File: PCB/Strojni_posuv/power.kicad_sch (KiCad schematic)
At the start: 0 parts

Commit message: PCB making #1 Power management
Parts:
- added 5V1: 5V, TestPoint:TestPoint_Pad_D1.5mm, symbol Connector:TestPoint
- added C15, C16: 1u, Capacitor_SMD:C_0402_1005Metric, symbol Device:C
- added D1: LED, LED_SMD:LED_0603_1608Metric, symbol Device:LED
- added JP1: SolderJumper_2_Open, Jumper:SolderJumper-2_P1.3mm_Open_TrianglePad1.0x1.5mm, symbol Jumper:SolderJumper_2_Open
- added R12: 510, Resistor_SMD:R_0402_1005Metric, symbol Device:R
- added U2: ~, Package_SO:SOIC-8-1EP_3.9x4.9mm_P1.27mm_EP2.29x3mm, symbol MP9486:MP9486AGN-Z
- added U4: MIC5365-3.3YC5, Package_TO_SOT_SMD:SOT-353_SC-70-5, symbol Regulator_Linear:MIC5365-3.3YC5
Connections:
- new net: D1.1 (K), R12.1
- new net: D1.2 (A), JP1.2 (B)
- new net +3.3V: C16.2, JP1.1 (A), U4.5 (VOUT)
- new net +5V: 5V1.1, C15.2, U4.1 (VIN), U4.3 (EN)
- new net GND: C15.1, C16.1, R12.2, U4.2 (GND)
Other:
- note added: "300mA"
- note added: "5V to 3.3V"
- note added: "Power LED"

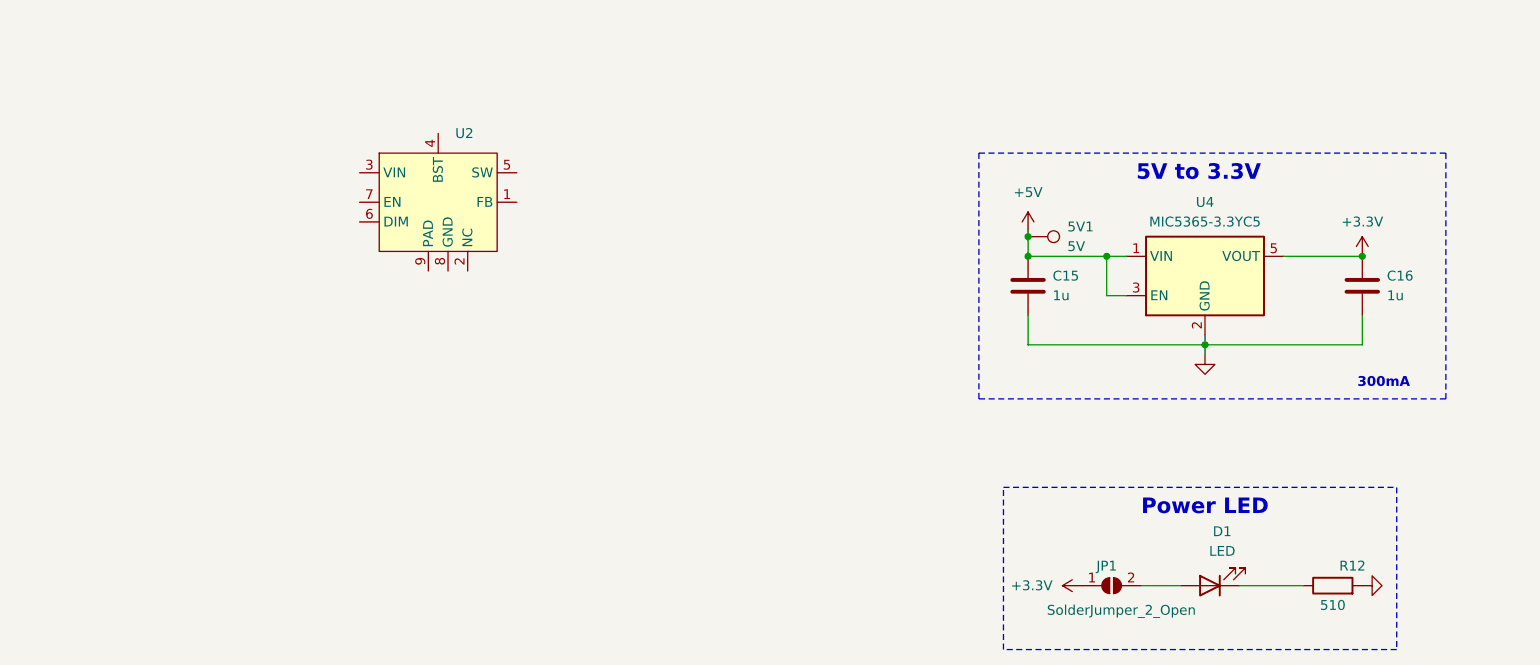
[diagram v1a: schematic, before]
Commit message: Learning, PCB making #2 Added new links to Learning Motor driver part in Kicad, Power part (48V to 5V), New pins to STM32F103
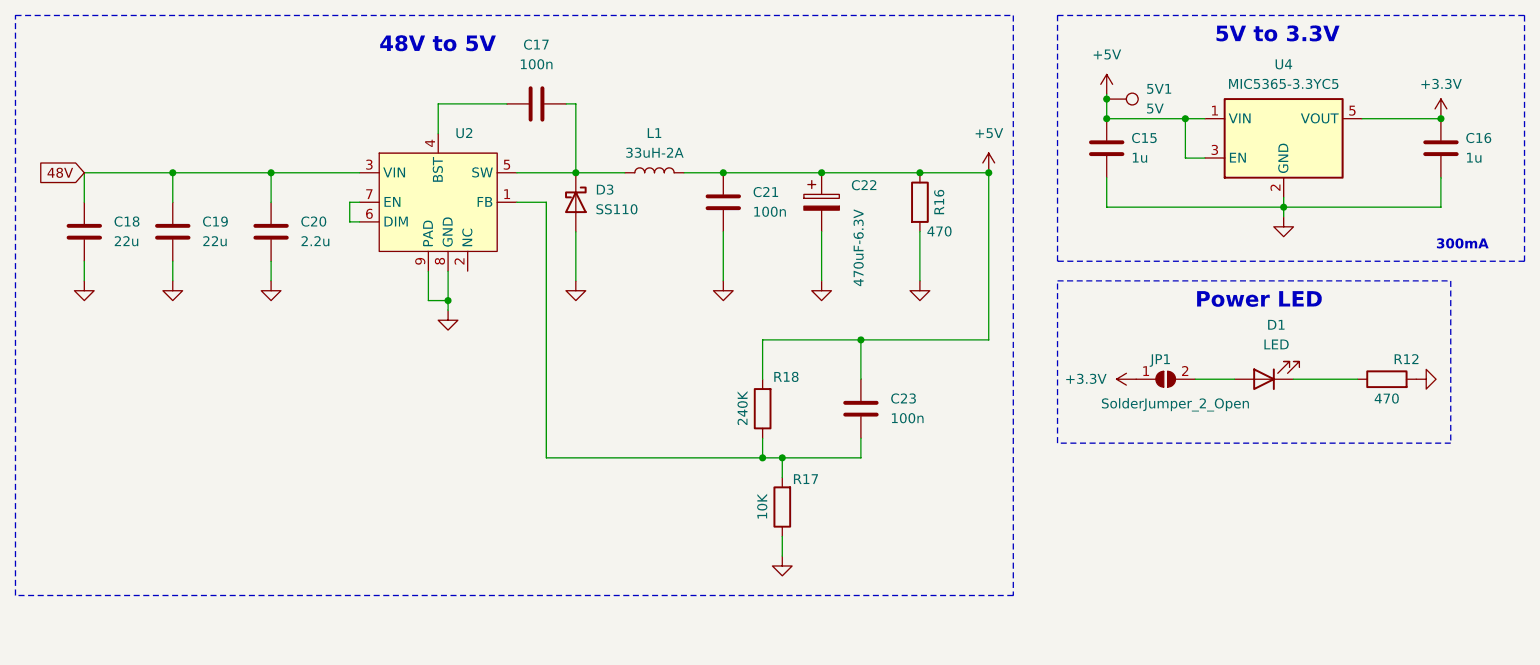
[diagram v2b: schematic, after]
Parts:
- added C17, C21, C23: 100n, symbol Device:C
- added C18, C19: 22u, symbol Device:C
- added C20: 2.2u, symbol Device:C
- added C22: 470uF-6.3V, symbol Device:C_Polarized
- added D3: SS110, symbol Device:D_Schottky
- added L1: 33uH-2A, symbol Device:L
- added R16: 470, symbol Device:R
- added R17: 10K, symbol Device:R
- added R18: 240K, symbol Device:R
- R12: value 510 -> 470
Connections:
- net +5V: now also C21.2, C22.1, C23.2, L1.2, R16.1, R18.2
- net GND: now also U2.8 (GND), U2.9 (PAD), C18.2, C19.2, C20.2, C21.1, C22.2, D3.2 (A), R16.2, R17.1
- net at U2.1 (FB): now also C23.1, R17.2, R18.1
- net 48V: now reaches U2.3 (VIN)
- net 48V: now also C18.1, C19.1, C20.1
- net at U2.4 (BST): now also C17.1
- net at U2.5 (SW): now also C17.2, D3.1 (K), L1.1
- net at U2.6 (DIM): now also U2.7 (EN)
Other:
- note added: "48V to 5V"
- moved on the sheet: 5V1, C15, C16, D1, JP1, R12, U4

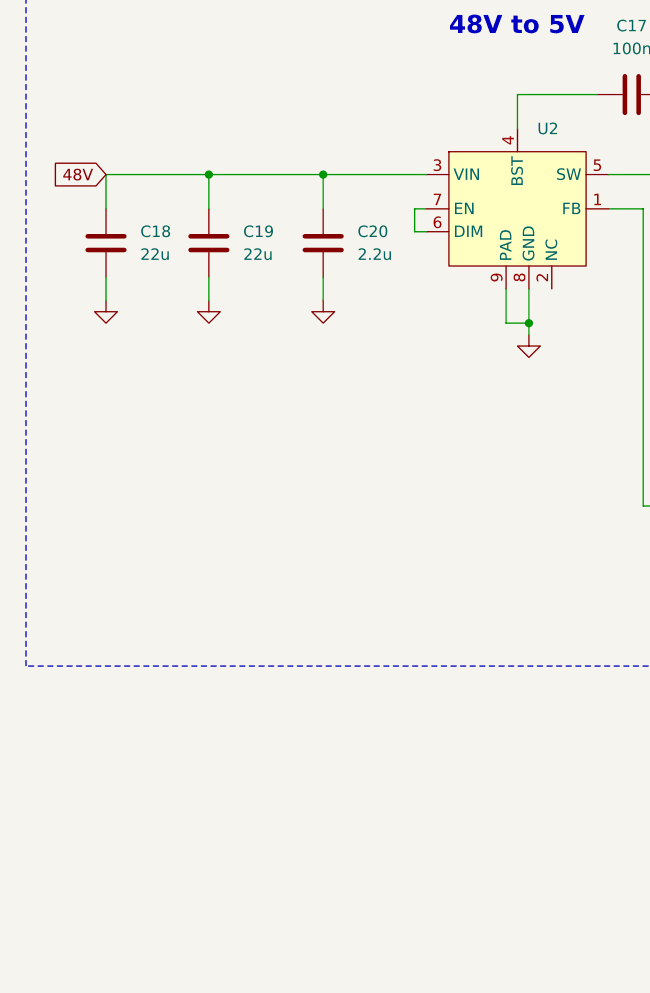
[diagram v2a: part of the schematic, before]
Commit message: PCB making #3 Whole motor driver, small power changes, STM32 clock and new pin configuration
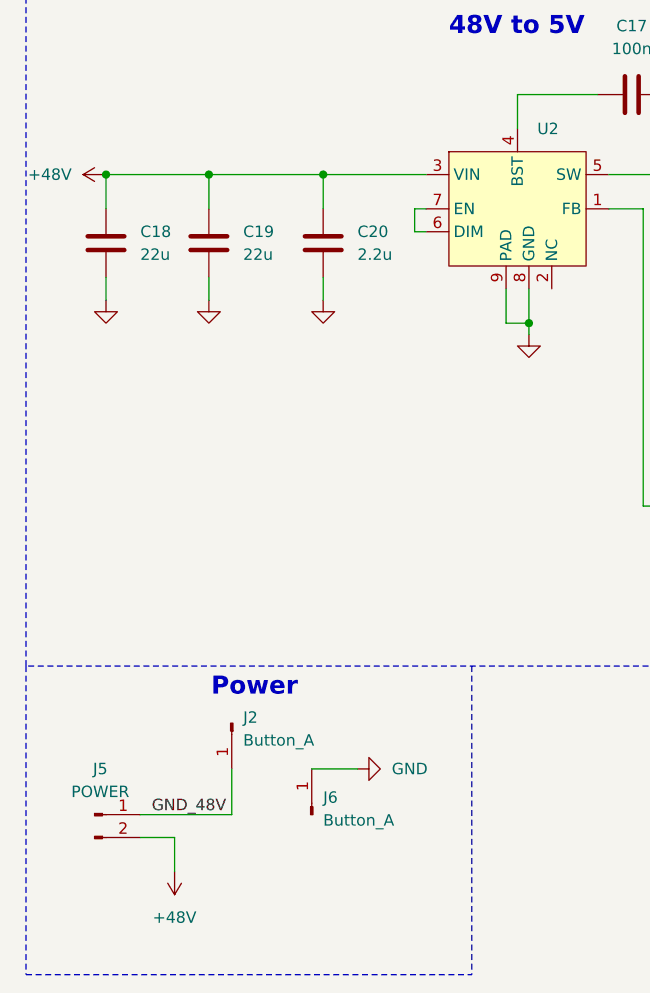
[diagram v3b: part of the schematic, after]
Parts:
- added J2, J6: Button_A, Connector_Pin:Pin_D1.3mm_L11.3mm_W2.8mm_Flat, symbol Connector:Conn_01x01_Pin
- added J5: POWER, Connector_AMASS:AMASS_XT60-M_1x02_P7.20mm_Vertical, symbol Connector:Conn_01x02_Pin
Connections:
- net GND: now also J6.1 (Pin_1)
- net 48V renamed +48V
- net +48V: now also J5.2 (Pin_2)
- new net GND_48V: J2.1 (Pin_1), J5.1 (Pin_1)
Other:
- note added: "Power"

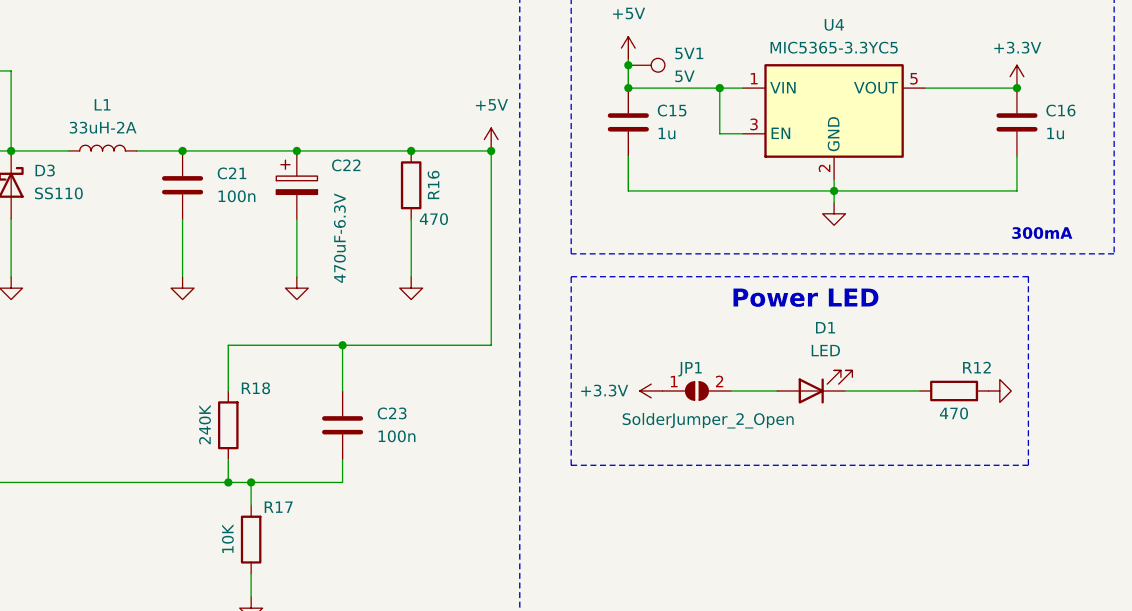
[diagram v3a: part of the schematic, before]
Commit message: PCB making #4 Finding components on JLCPCB and adding their tags to schematic. Assigning almost all footprints
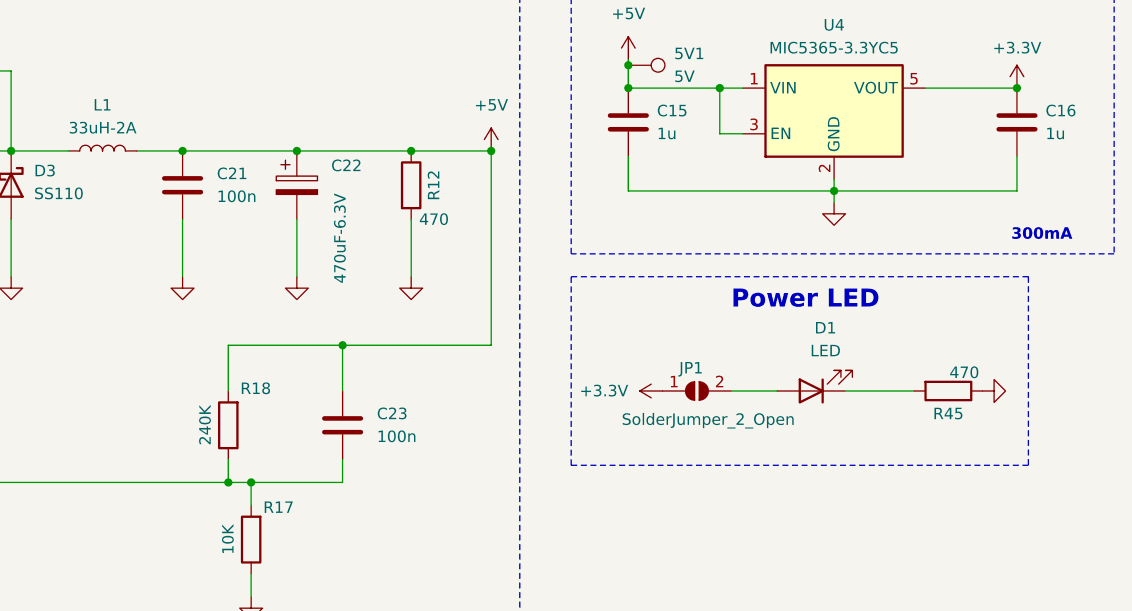
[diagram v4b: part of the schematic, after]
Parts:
- removed R16: 470, symbol Device:R
- added R45: 470, Resistor_SMD:R_0603_1608Metric, symbol Device:R
- C15, C16: footprint Capacitor_SMD:C_0402_1005Metric -> Capacitor_SMD:C_0603_1608Metric; LCSC C412453 -> C15849
- C17, C21, C23: footprint (none) -> Capacitor_SMD:C_0603_1608Metric; LCSC (none) -> C14663
- C18, C19: footprint (none) -> Capacitor_SMD:C_2220_5750Metric; LCSC (none) -> C784103
- C20: footprint (none) -> Capacitor_SMD:C_0805_2012Metric; LCSC (none) -> C513763
- C22: footprint (none) -> Capacitor_SMD:CP_Elec_6.3x7.7; LCSC (none) -> C114446
- D3: footprint (none) -> Diode_SMD:D_SMA; LCSC (none) -> C2482
- L1: footprint (none) -> Inductor_SMD:L_Sunlord_MWSA0603S; LCSC (none) -> C408454
- R12: footprint Resistor_SMD:R_0402_1005Metric -> Resistor_SMD:R_0603_1608Metric; LCSC C103085 -> C23179
- R17: footprint (none) -> Resistor_SMD:R_0603_1608Metric; LCSC (none) -> C25804
- R18: footprint (none) -> Resistor_SMD:R_0603_1608Metric; LCSC (none) -> C4197
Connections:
- net +5V: now also C21.1, C23.1, R12.1; no longer C21.2, C23.2
- net GND: now also C21.2, R45.1; no longer C21.1
- net at R17.2, R18.1, U2.1 (FB): now also C23.2; no longer C23.1
- net at D1.1 (K): now also R45.2; no longer R12.1

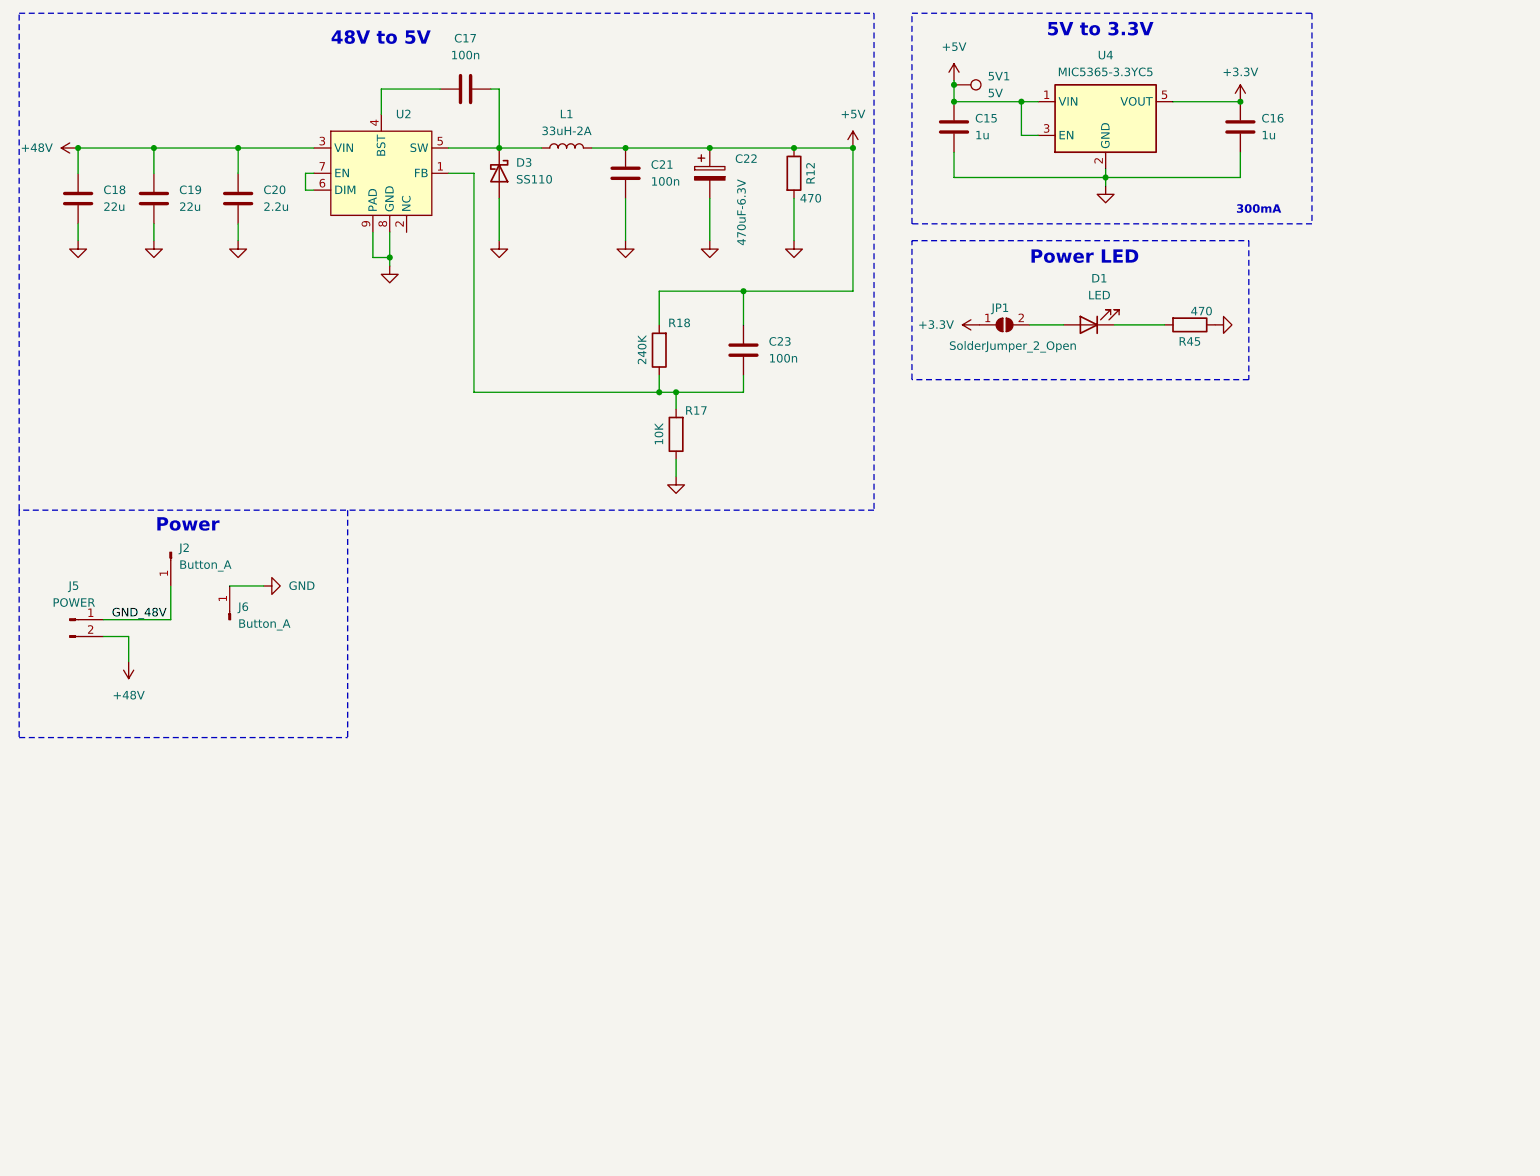
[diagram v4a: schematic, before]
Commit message: PCB making #6 Placing all components - component layout
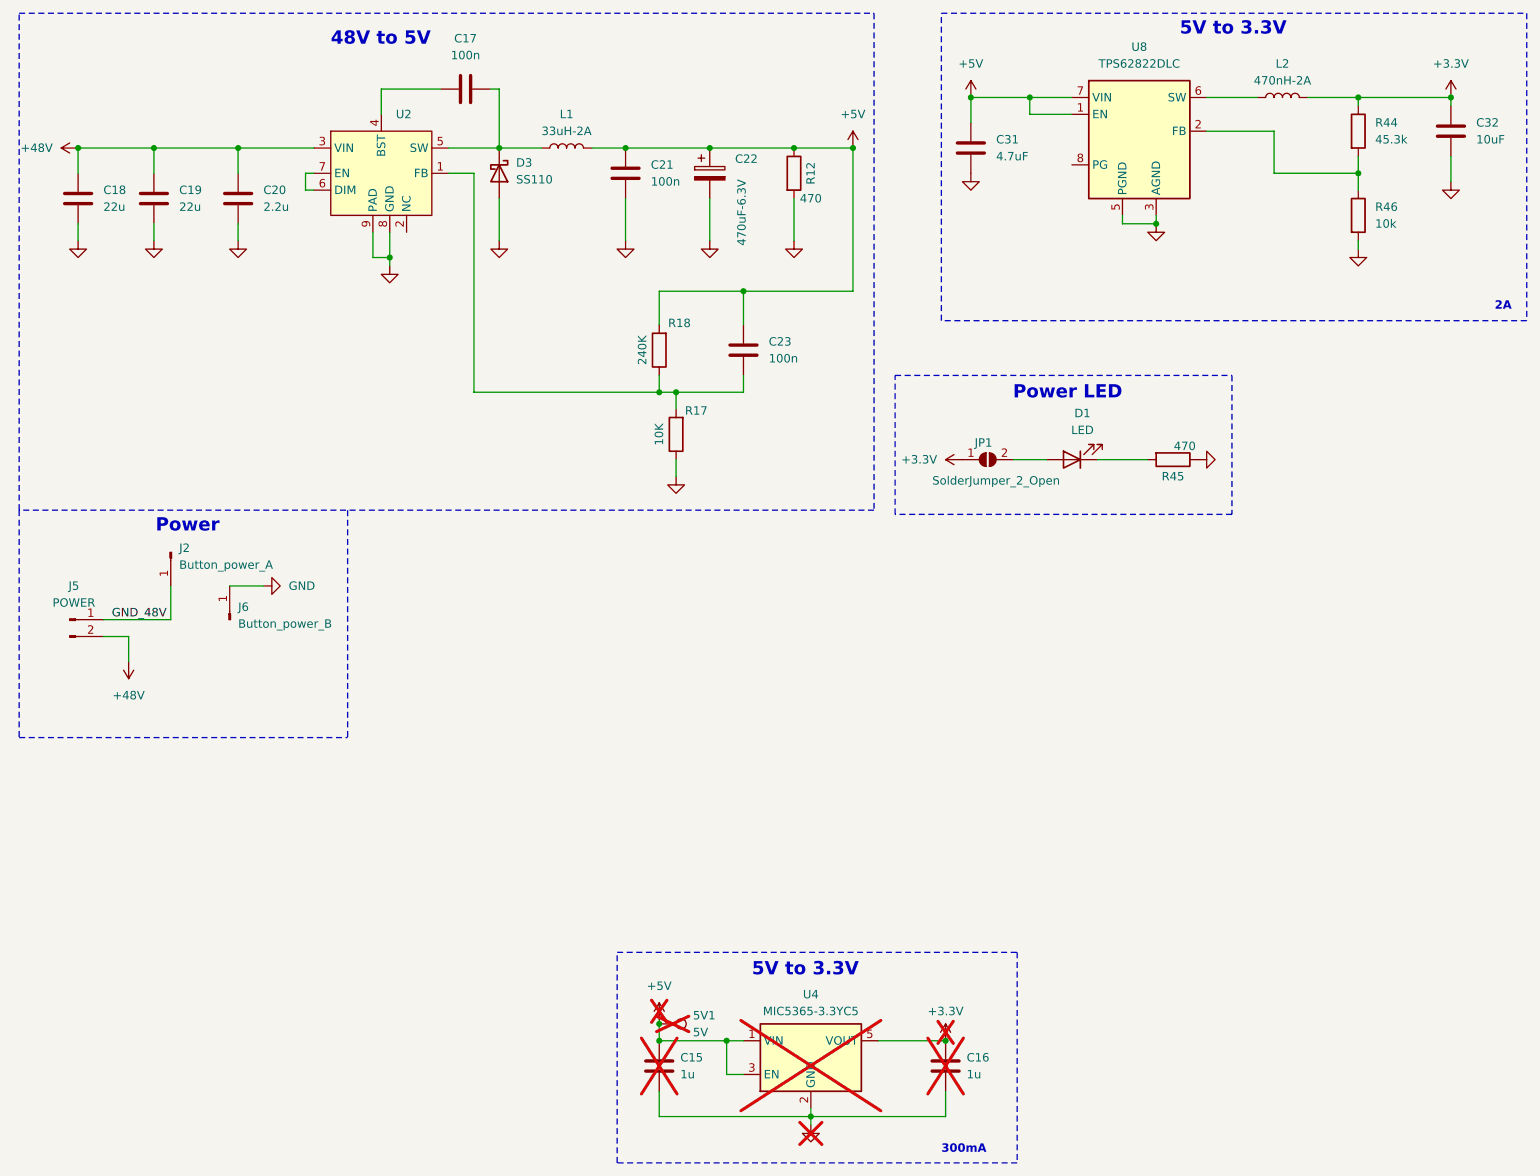
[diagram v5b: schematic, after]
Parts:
- added C31: 4.7uF, Capacitor_SMD:C_0603_1608Metric, symbol Device:C
- added C32: 10uF, Capacitor_SMD:C_0603_1608Metric, symbol Device:C
- added L2: 470nH-2A, Inductor_SMD:L_1008_2520Metric, symbol Device:L
- added R44: 45.3k, Resistor_SMD:R_0603_1608Metric, symbol Device:R
- added R46: 10k, Resistor_SMD:R_0603_1608Metric, symbol Device:R
- added U8: TPS62822DLC, Package_SON:Texas_VSON-HR-8_1.5x2mm_P0.5mm, symbol Regulator_Switching:TPS62822DLC
- 5V1, C15, C16, U4: now not fitted; now left out of the parts list
- J2: value Button_A -> Button_power_A
- J6: value Button_A -> Button_power_B
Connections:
- net +3.3V: now also C32.1, L2.2, R44.1
- net +5V: now also C31.1, U8.1 (EN), U8.7 (VIN)
- net GND: now also C31.2, C32.2, R46.2, U8.3 (AGND), U8.5 (PGND)
- new net: R44.2, R46.1, U8.2 (FB)
- new net: L2.1, U8.6 (SW)
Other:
- note added: "2A"
- moved on the sheet: D1, JP1, R45

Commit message: Revision 0
The PCB is done
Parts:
- R46: value 10k -> 10K
- U2: LCSC (none) -> C404013
